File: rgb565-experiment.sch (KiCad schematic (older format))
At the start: 32 parts, among them J1 ST_SHIFTER_SOCKET, SW1 SW_SPDT, U1 74HC00, U2 ST_SHIFTER, U3 ST_SHIFTER, U4 74HC245, U5 74LS257, U6 74HC245

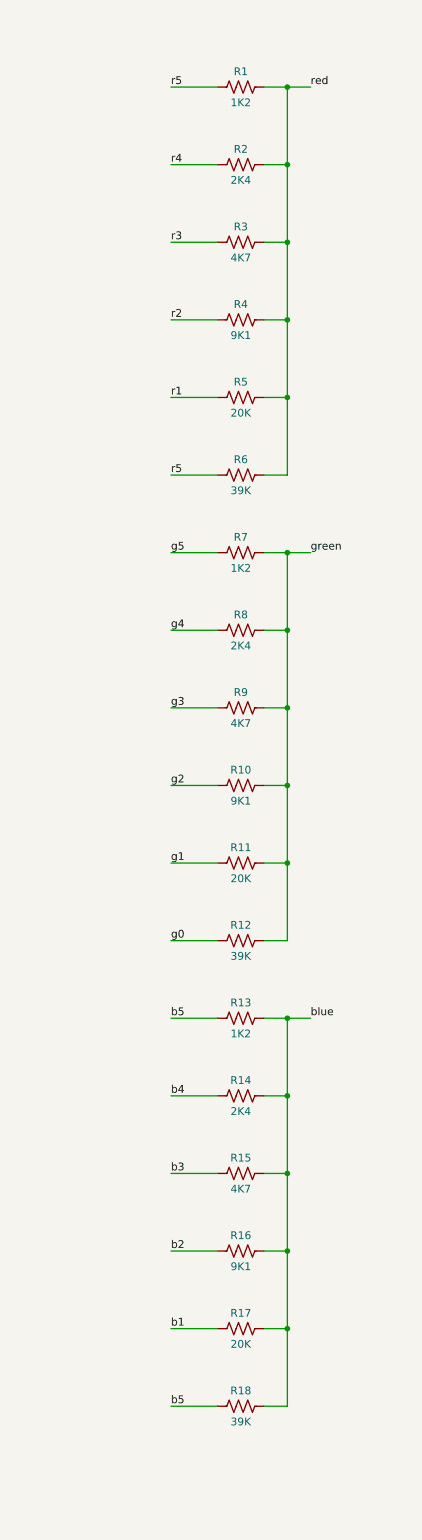
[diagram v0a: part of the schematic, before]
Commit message: fixed the resistor values to match the original mod
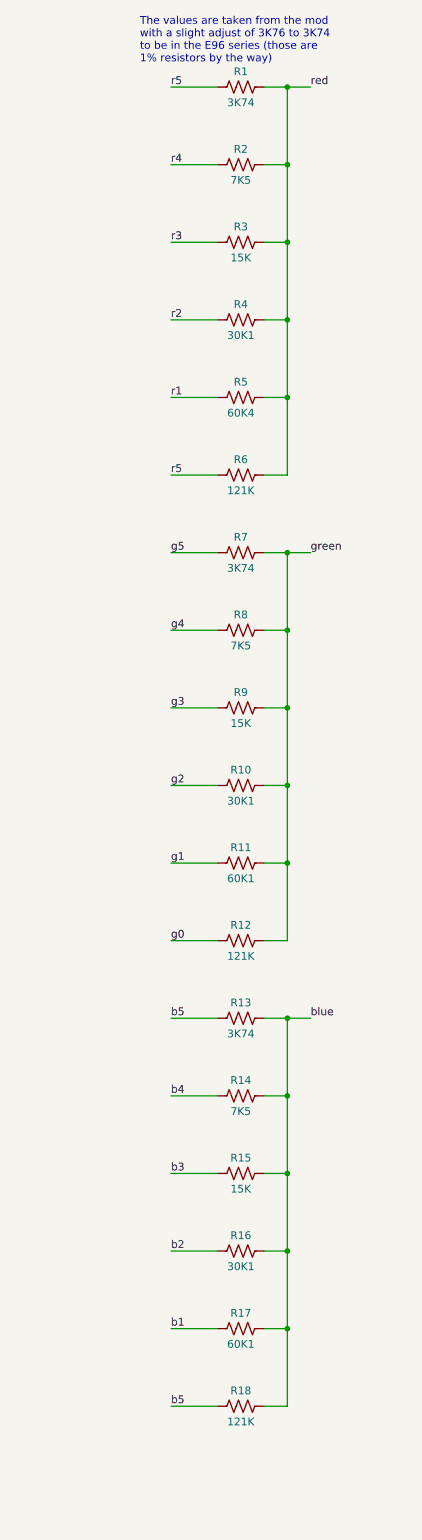
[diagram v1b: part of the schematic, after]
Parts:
- R1, R13, R7: value 1K2 -> 3K74
- R10, R16, R4: value 9K1 -> 30K1
- R11, R17: value 20K -> 60K1
- R12, R18, R6: value 39K -> 121K
- R14, R2, R8: value 2K4 -> 7K5
- R15, R3, R9: value 4K7 -> 15K
- R5: value 20K -> 60K4
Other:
- note added: "The values are taken from the mod\nwith a slight adjust of 3K76 to 3K74\nto be in the E96 series (those are\n1% resistors by the way)"
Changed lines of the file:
@@
 P 15000 1000
 F 0 "R1" V 15100 1000 50  0000 C CNN
-F 1 "1K2" V 14900 1000 50  0000 C CNN
+F 1 "3K74" V 14900 1000 50  0000 C CNN
 F 2 "" V 15040 990 50  0001 C CNN
 F 3 "~" H 15000 1000 50  0001 C CNN
@@
 P 15000 1500
 F 0 "R2" V 15100 1500 50  0000 C CNN
-F 1 "2K4" V 14900 1500 50  0000 C CNN
+F 1 "7K5" V 14900 1500 50  0000 C CNN
 F 2 "" V 15040 1490 50  0001 C CNN
 F 3 "~" H 15000 1500 50  0001 C CNN
@@
 P 15000 2000
 F 0 "R3" V 15100 2000 50  0000 C CNN
-F 1 "4K7" V 14900 2000 50  0000 C CNN
+F 1 "15K" V 14900 2000 50  0000 C CNN
 F 2 "" V 15040 1990 50  0001 C CNN
 F 3 "~" H 15000 2000 50  0001 C CNN
@@
 P 15000 2500
 F 0 "R4" V 15100 2500 50  0000 C CNN
-F 1 "9K1" V 14900 2500 50  0000 C CNN
+F 1 "30K1" V 14900 2500 50  0000 C CNN
 F 2 "" V 15040 2490 50  0001 C CNN
 F 3 "~" H 15000 2500 50  0001 C CNN
@@
 P 15000 3000
 F 0 "R5" V 15100 3000 50  0000 C CNN
-F 1 "20K" V 14900 3000 50  0000 C CNN
+F 1 "60K4" V 14900 3000 50  0000 C CNN
 F 2 "" V 15040 2990 50  0001 C CNN
 F 3 "~" H 15000 3000 50  0001 C CNN
@@
 P 15000 3500
 F 0 "R6" V 15100 3500 50  0000 C CNN
-F 1 "39K" V 14900 3500 50  0000 C CNN
+F 1 "121K" V 14900 3500 50  0000 C CNN
 F 2 "" V 15040 3490 50  0001 C CNN
 F 3 "~" H 15000 3500 50  0001 C CNN
@@
 P 15000 4000
 F 0 "R7" V 15100 4000 50  0000 C CNN
-F 1 "1K2" V 14900 4000 50  0000 C CNN
+F 1 "3K74" V 14900 4000 50  0000 C CNN
 F 2 "" V 15040 3990 50  0001 C CNN
 F 3 "~" H 15000 4000 50  0001 C CNN
@@
 P 15000 4500
 F 0 "R8" V 15100 4500 50  0000 C CNN
-F 1 "2K4" V 14900 4500 50  0000 C CNN
+F 1 "7K5" V 14900 4500 50  0000 C CNN
 F 2 "" V 15040 4490 50  0001 C CNN
 F 3 "~" H 15000 4500 50  0001 C CNN
@@
 P 15000 5000
 F 0 "R9" V 15100 5000 50  0000 C CNN
-F 1 "4K7" V 14900 5000 50  0000 C CNN
+F 1 "15K" V 14900 5000 50  0000 C CNN
 F 2 "" V 15040 4990 50  0001 C CNN
 F 3 "~" H 15000 5000 50  0001 C CNN
@@
 P 15000 5500
 F 0 "R10" V 15100 5500 50  0000 C CNN
-F 1 "9K1" V 14900 5500 50  0000 C CNN
+F 1 "30K1" V 14900 5500 50  0000 C CNN
 F 2 "" V 15040 5490 50  0001 C CNN
 F 3 "~" H 15000 5500 50  0001 C CNN
@@
 P 15000 6000
 F 0 "R11" V 15100 6000 50  0000 C CNN
-F 1 "20K" V 14900 6000 50  0000 C CNN
+F 1 "60K1" V 14900 6000 50  0000 C CNN
 F 2 "" V 15040 5990 50  0001 C CNN
 F 3 "~" H 15000 6000 50  0001 C CNN
@@
 P 15000 6500
 F 0 "R12" V 15100 6500 50  0000 C CNN
-F 1 "39K" V 14900 6500 50  0000 C CNN
+F 1 "121K" V 14900 6500 50  0000 C CNN
 F 2 "" V 15040 6490 50  0001 C CNN
 F 3 "~" H 15000 6500 50  0001 C CNN
@@
 P 15000 7000
 F 0 "R13" V 15100 7000 50  0000 C CNN
-F 1 "1K2" V 14900 7000 50  0000 C CNN
+F 1 "3K74" V 14900 7000 50  0000 C CNN
 F 2 "" V 15040 6990 50  0001 C CNN
 F 3 "~" H 15000 7000 50  0001 C CNN
@@
 P 15000 7500
 F 0 "R14" V 15100 7500 50  0000 C CNN
-F 1 "2K4" V 14900 7500 50  0000 C CNN
+F 1 "7K5" V 14900 7500 50  0000 C CNN
 F 2 "" V 15040 7490 50  0001 C CNN
 F 3 "~" H 15000 7500 50  0001 C CNN
@@
 P 15000 8000
 F 0 "R15" V 15100 8000 50  0000 C CNN
-F 1 "4K7" V 14900 8000 50  0000 C CNN
+F 1 "15K" V 14900 8000 50  0000 C CNN
 F 2 "" V 15040 7990 50  0001 C CNN
 F 3 "~" H 15000 8000 50  0001 C CNN
@@
 P 15000 8500
 F 0 "R16" V 15100 8500 50  0000 C CNN
-F 1 "9K1" V 14900 8500 50  0000 C CNN
+F 1 "30K1" V 14900 8500 50  0000 C CNN
 F 2 "" V 15040 8490 50  0001 C CNN
 F 3 "~" H 15000 8500 50  0001 C CNN
@@
 P 15000 9000
 F 0 "R17" V 15100 9000 50  0000 C CNN
-F 1 "20K" V 14900 9000 50  0000 C CNN
+F 1 "60K1" V 14900 9000 50  0000 C CNN
 F 2 "" V 15040 8990 50  0001 C CNN
 F 3 "~" H 15000 9000 50  0001 C CNN
@@
 P 15000 9500
 F 0 "R18" V 15100 9500 50  0000 C CNN
-F 1 "39K" V 14900 9500 50  0000 C CNN
+F 1 "121K" V 14900 9500 50  0000 C CNN
 F 2 "" V 15040 9490 50  0001 C CNN
 F 3 "~" H 15000 9500 50  0001 C CNN
@@
 Text Notes 5300 3950 0    50   ~ 0
 «Additionally, jumpers are installed across \neach of three 3.6K ohm resistors on the motherboard.  \nThese resistors are easily traced from the Shifter \nsocket pins 21, 24, and 27.» \n(From the original text)\n
+Text Notes 14350 850  0    50   ~ 0
+The values are taken from the mod\nwith a slight adjust of 3K76 to 3K74\nto be in the E96 series (those are\n1% resistors by the way)
 $EndSCHEMATC

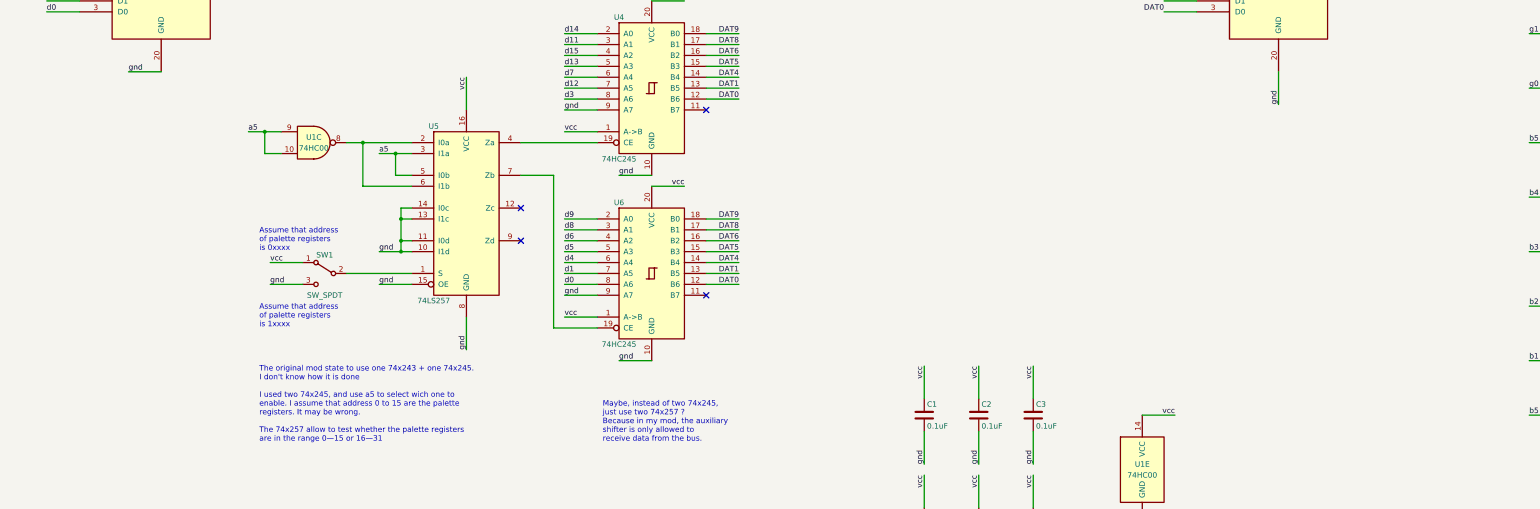
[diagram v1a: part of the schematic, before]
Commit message: add additionnal connectors : supplemental power, digital 18bits signal
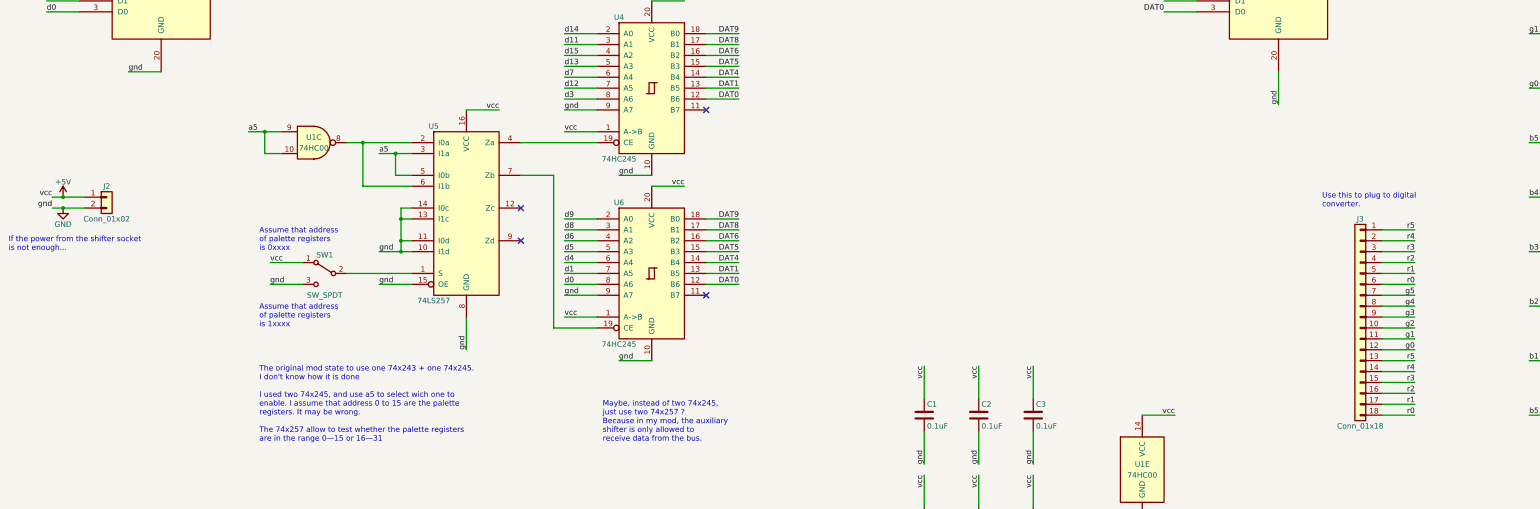
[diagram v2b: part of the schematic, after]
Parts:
- added J2: Conn_01x02, symbol Connector_Generic:Conn_01x02
- added J3: Conn_01x18, symbol Connector_Generic:Conn_01x18
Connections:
- net g0: now also J3.12 (Pin_12)
- net g1: now also J3.11 (Pin_11)
- net g2: now also J3.10 (Pin_10)
- net g3: now also J3.9 (Pin_9)
- net g4: now also J3.8 (Pin_8)
- net g5: now also J3.7 (Pin_7)
- net r1: now also J3.17 (Pin_17), J3.5 (Pin_5)
- net r2: now also J3.16 (Pin_16), J3.4 (Pin_4)
- net r3: now also J3.15 (Pin_15), J3.3 (Pin_3)
- net r4: now also J3.14 (Pin_14), J3.2 (Pin_2)
- net r5: now also J3.1 (Pin_1), J3.13 (Pin_13)
- net gnd renamed GND
- net GND: now also J2.2 (Pin_2)
- net vcc renamed +5V
- net +5V: now also J2.1 (Pin_1)
- new net r0: J3.18 (Pin_18), J3.6 (Pin_6)
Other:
- note added: "If the power from the shifter socket\nis not enough..."
- note added: "Use this to plug to digital\nconverter."
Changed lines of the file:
@@
 Sheet 1 1
 Title "Experimental RGB-565 mod for the Atari ST"
-Date "2021-12-15"
-Rev "v1.0.0-exp1"
+Date "2021-12-16"
+Rev "v1.0.0-exp2"
 Comp "Sporniket-Studio.com"
 Comment1 ""
@@
 Wire Wire Line
 	4800 8900 4800 8600
-Text Label 4800 6400 3    50   ~ 0
-vcc
-Wire Wire Line
-	4800 6700 4800 6400
+Text Label 5100 6700 2    50   ~ 0
+vcc
+Wire Wire Line
+	4800 6700 5100 6700
 Wire Wire Line
 	2950 6900 2950 7100
@@
 Text Notes 14350 850  0    50   ~ 0
 The values are taken from the mod\nwith a slight adjust of 3K76 to 3K74\nto be in the E96 series (those are\n1% resistors by the way)
+$Comp
+L Connector_Generic:Conn_01x02 J2
+U 1 1 61BD19F2
+P 1500 7500
+F 0 "J2" H 1500 7600 50  0000 C CNN
+F 1 "Conn_01x02" H 1500 7300 50  0000 C CNN
+F 2 "" H 1500 7500 50  0001 C CNN
+F 3 "~" H 1500 7500 50  0001 C CNN
+	1    1500 7500
+	1    0    0    -1
+$EndComp
+Text Label 1000 7500 2    50   ~ 0
+vcc
+Text Label 1000 7600 2    50   ~ 0
+gnd
+Wire Wire Line
+	1000 7600 1100 7600
+Wire Wire Line
+	1000 7500 1100 7500
+$Comp
+L power:GND #PWR02
+U 1 1 61C17A12
+P 1100 7600
+F 0 "#PWR02" H 1100 7350 50  0001 C CNN
+F 1 "GND" H 1100 7450 50  0000 C CNN
+F 2 "" H 1100 7600 50  0001 C CNN
+F 3 "" H 1100 7600 50  0001 C CNN
+	1    1100 7600
+	1    0    0    -1
+$EndComp
+Connection ~ 1100 7600
+Wire Wire Line
+	1100 7600 1300 7600
+$Comp
+L power:+5V #PWR01
+U 1 1 61C185E7
+P 1100 7500
+F 0 "#PWR01" H 1100 7350 50  0001 C CNN
+F 1 "+5V" H 1100 7640 50  0000 C CNN
+F 2 "" H 1100 7500 50  0001 C CNN
+F 3 "" H 1100 7500 50  0001 C CNN
+	1    1100 7500
+	1    0    0    -1
+$EndComp
+Connection ~ 1100 7500
+Wire Wire Line
+	1100 7500 1300 7500
+Text Notes 600  8000 0    50   ~ 0
+If the power from the shifter socket\nis not enough...
+$Comp
+L Connector_Generic:Conn_01x18 J3
+U 1 1 61C19D2C
+P 13000 8600
+F 0 "J3" H 13000 9500 50  0000 C CNN
+F 1 "Conn_01x18" H 13000 7600 50  0000 C CNN
+F 2 "" H 13000 8600 50  0001 C CNN
+F 3 "~" H 13000 8600 50  0001 C CNN
+	1    13000 8600
+	-1   0    0    -1
+$EndComp
+Text Label 13500 8300 2    50   ~ 0
+r0
+Text Label 13500 8200 2    50   ~ 0
+r1
+Text Label 13500 8100 2    50   ~ 0
+r2
+Text Label 13500 8000 2    50   ~ 0
+r3
+Text Label 13500 7900 2    50   ~ 0
+r4
+Text Label 13500 7800 2    50   ~ 0
+r5
+Text Label 13500 8900 2    50   ~ 0
+g0
+Text Label 13500 8800 2    50   ~ 0
+g1
+Text Label 13500 8700 2    50   ~ 0
+g2
+Text Label 13500 8600 2    50   ~ 0
+g3
+Text Label 13500 8500 2    50   ~ 0
+g4
+Text Label 13500 8400 2    50   ~ 0
+g5
+Text Label 13500 9500 2    50   ~ 0
+r0
+Text Label 13500 9400 2    50   ~ 0
+r1
+Text Label 13500 9300 2    50   ~ 0
+r2
+Text Label 13500 9200 2    50   ~ 0
+r3
+Text Label 13500 9100 2    50   ~ 0
+r4
+Text Label 13500 9000 2    50   ~ 0
+r5
+Wire Wire Line
+	13200 7800 13500 7800
+Wire Wire Line
+	13200 7900 13500 7900
+Wire Wire Line
+	13200 8000 13500 8000
+Wire Wire Line
+	13200 8100 13500 8100
+Wire Wire Line
+	13200 8200 13500 8200
+Wire Wire Line
+	13200 8300 13500 8300
+Wire Wire Line
+	13200 8400 13500 8400
+Wire Wire Line
+	13200 8500 13500 8500
+Wire Wire Line
+	13200 8600 13500 8600
+Wire Wire Line
+	13200 8700 13500 8700
+Wire Wire Line
+	13200 8800 13500 8800
+Wire Wire Line
+	13200 8900 13500 8900
+Wire Wire Line
+	13200 9000 13500 9000
+Wire Wire Line
+	13200 9100 13500 9100
+Wire Wire Line
+	13200 9200 13500 9200
+Wire Wire Line
+	13200 9300 13500 9300
+Wire Wire Line
+	13200 9400 13500 9400
+Wire Wire Line
+	13200 9500 13500 9500
+Text Notes 12650 7600 0    50   ~ 0
+Use this to plug to digital\nconverter.
 $EndSCHEMATC

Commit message: assign footprints
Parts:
- C1, C2, C3, C4, C5, C6: footprint (none) -> commons-passives_THT:Passive_THT_capacitor_mlcc_W2.54mm_L7.62mm
- J1, U2, U3: footprint Package_DIP:DIP-40_W15.24mm_LongPads -> Package_DIP:DIP-40_W15.24mm_Socket
- J2: footprint (none) -> Connector_PinHeader_2.54mm:PinHeader_1x02_P2.54mm_Vertical
- J3: footprint (none) -> Connector_PinHeader_2.54mm:PinHeader_1x18_P2.54mm_Vertical
- R1, R10, R11, R12, R13, R14, R15, R16, R17, R18, R2, R3, R4, R5, R6, R7, R8, R9: footprint (none) -> commons-passives_THT:Passive_THT_resistor_W2.54mm_L10.16mm
- SW1: footprint (none) -> Connector_PinHeader_2.54mm:PinHeader_1x03_P2.54mm_Vertical
- U1: footprint (none) -> Package_DIP:DIP-14_W7.62mm_Socket
- U4, U6: footprint (none) -> Package_DIP:DIP-20_W7.62mm_Socket
- U5: footprint (none) -> Package_DIP:DIP-16_W7.62mm_Socket

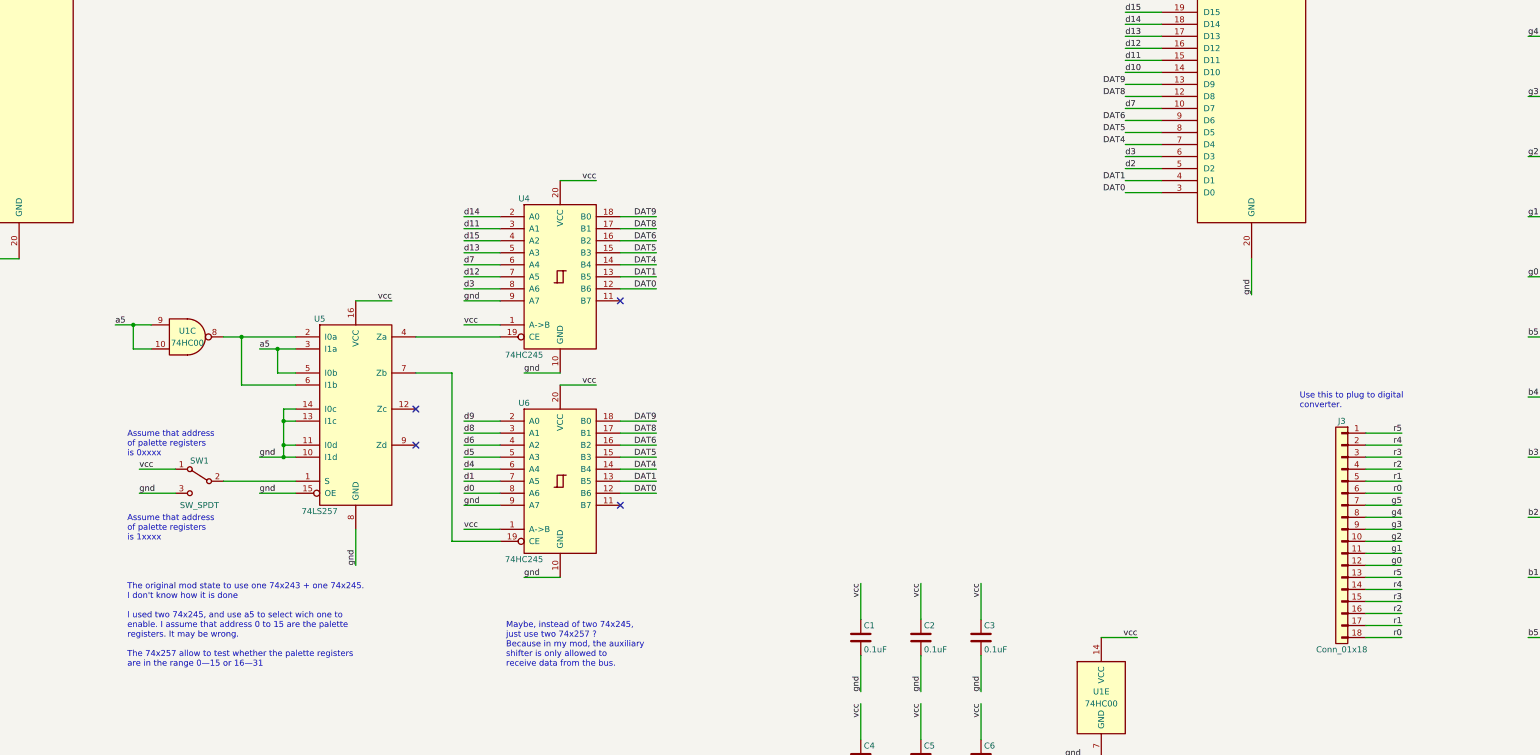
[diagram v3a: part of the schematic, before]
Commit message: added pull-up for data, removed redundant connector to digital signal, continue tracing
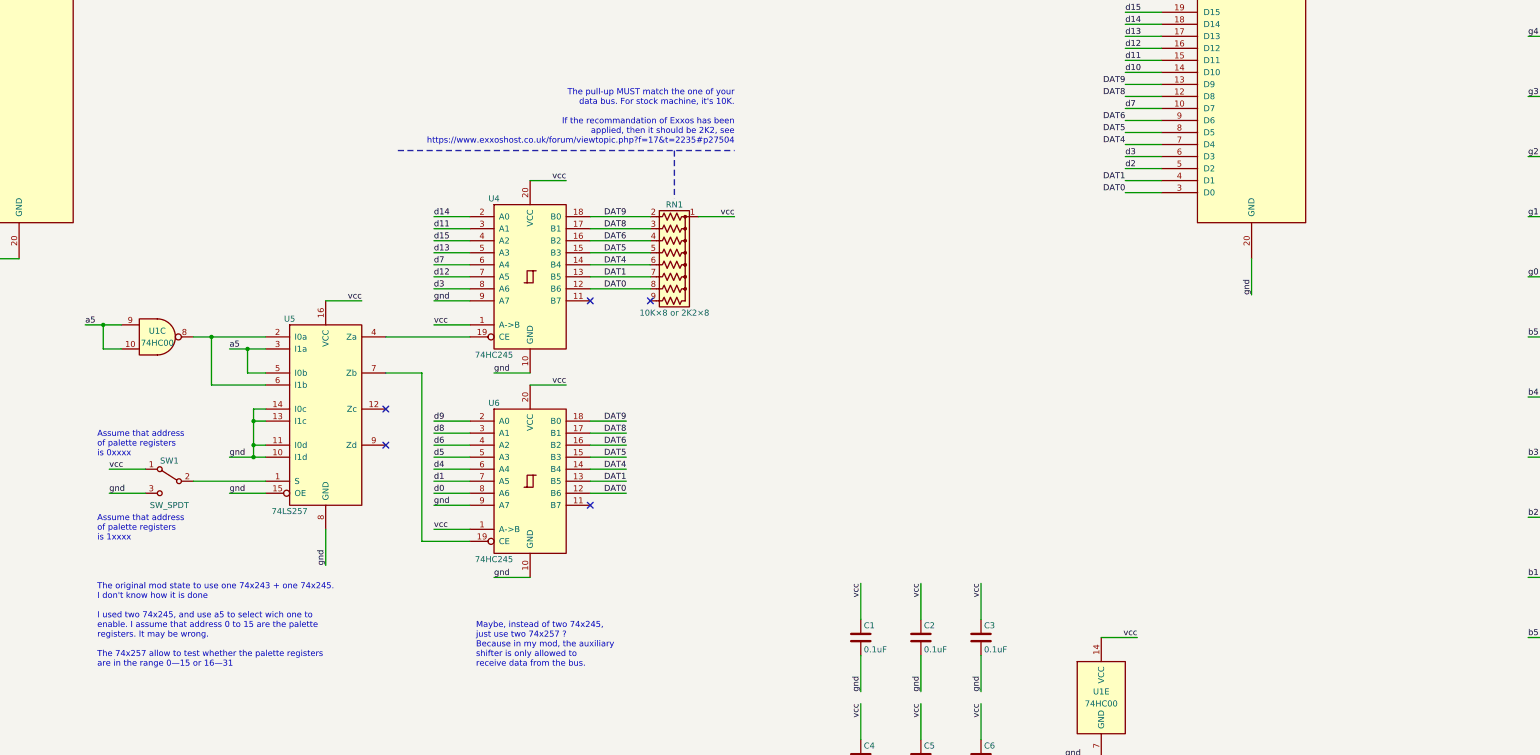
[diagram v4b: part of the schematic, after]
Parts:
- removed J3: Conn_01x18, Connector_PinHeader_2.54mm:PinHeader_1x18_P2.54mm_Vertical, symbol Connector_Generic:Conn_01x18
- added RN1: 10K×8 or 2K2×8, Resistor_THT:R_Array_SIP9, symbol Device:R_Network08_US
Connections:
- net +5V: now also RN1.1 (common)
- net DAT0: now also RN1.8 (R7)
- net DAT1: now also RN1.7 (R6)
- net DAT4: now also RN1.6 (R5)
- net DAT5: now also RN1.5 (R4)
- net DAT6: now also RN1.4 (R3)
- net DAT8: now also RN1.3 (R2)
- net DAT9: now also RN1.2 (R1)
- no-connect marks 14 -> 15
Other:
- note added: "The pull-up MUST match the one of your\ndata bus. For stock machine, it's 10K.\n\nIf the recommandation of Exxos has been\napplied, then it should be 2K2, see\nhttps://www.exxoshost.co.uk/forum/viewtopic.php?f=17&t=2235#p27504"
- note removed: "Use this to plug to digital\nconverter."
- moved on the sheet: SW1, U1C, U4, U5, U6
